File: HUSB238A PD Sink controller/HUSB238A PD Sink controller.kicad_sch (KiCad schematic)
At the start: 28 parts, among them J1 Power out header, J2 VSET, J3 Power out terminal, J4 ISET, J6 I2C, Q1 PMOS, U1 SRV05-4, U2 HUSB238A-xxxxx-QN16R

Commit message: R2.3
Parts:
- removed J1: Power out header, Connector_PinHeader_2.54mm:PinHeader_1x02_P2.54mm_Vertical, symbol Connector:Conn_01x02_Pin
- removed Q1: PMOS, symbol Simulation_SPICE:PMOS
- removed U1: SRV05-4, Package_TO_SOT_SMD:SOT-23-6, symbol Power_Protection:SRV05-4
- added D1: ≥48V TVS Clamp, Diode_SMD:D_SOD-123F, symbol Device:D_TVS_Small
- added Q1: CJAC70P06, Package_DFN_QFN:PQFN-8-EP_6x5mm_P1.27mm_Generic, symbol CJAC70P06:CJAC70P06
- added R4: 900kΩ, Resistor_SMD:R_0603_1608Metric, symbol Device:R_Small
- added U1: TPD4E05U06DQA, Package_SON:USON-10_2.5x1.0mm_P0.5mm, symbol Power_Protection:TPD4E05U06DQA
- C1: footprint Capacitor_SMD:C_1206_3216Metric_Pad1.33x1.80mm_HandSolder -> Capacitor_SMD:C_0603_1608Metric; LCSC Part # (none) -> C15849
- D2: renamed from D1; value ~ -> 15V; footprint Diode_SMD:D_1206_3216Metric_Pad1.42x1.75mm_HandSolder -> Diode_SMD:D_SOD-323
- J1: renamed from J3; value Power out terminal -> VBUS
- JP1: renamed from JP3; value I2C Mode -> I2C Enabled
- R1: value ~ -> 100kΩ; footprint Resistor_SMD:R_1206_3216Metric_Pad1.30x1.75mm_HandSolder -> Resistor_SMD:R_0603_1608Metric; LCSC Part # (none) -> C25803
- R12: renamed from R13; LCSC Part # (none) -> C74154
- R13: renamed from R12; LCSC Part # (none) -> C43670
- R14: renamed from R11; LCSC Part # (none) -> C229764
- R15: renamed from R10; LCSC Part # (none) -> C18012
- R16: renamed from R9; LCSC Part # (none) -> C17888
- R2: value ~ -> 20kΩ; footprint Resistor_SMD:R_1206_3216Metric_Pad1.30x1.75mm_HandSolder -> Resistor_SMD:R_0603_1608Metric; LCSC Part # (none) -> C4184
- R3: renamed from R15; footprint Resistor_SMD:R_1206_3216Metric_Pad1.30x1.75mm_HandSolder -> Resistor_SMD:R_0603_1608Metric; LCSC Part # (none) -> C22935
- R5: renamed from R3; LCSC Part # (none) -> C17888
- R6: renamed from R4; LCSC Part # (none) -> C18012
- R7: renamed from R5; LCSC Part # (none) -> C229764
- R8: renamed from R6; LCSC Part # (none) -> C43670
- R9: renamed from R7; LCSC Part # (none) -> C74154
- U2: value HUSB238A-xxxxx-QN16R -> HUSB238A; LCSC Part # (none) -> C24833806
- USBC1: LCSC Part # (none) -> C2931470
- renumbered J6 to J3, R8 to R10, R14 to R11
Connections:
- net CC1: now also U1.4 (D2+), U1.7 (NC)
- net CC2: now also U1.5 (D2-), U1.6 (NC)
- net D+: now also U1.1 (D1+), U1.10 (NC)
- net D-: now also U1.2 (D1-), U1.9 (NC)
- net GND: now also J1.1 (Pin_1), JP2.3, D1.2 (A2), U1.3 (GND), U1.8 (GND); no longer J1.2 (Pin_2), JP2.1 (42H)
- net GPIO/I2C: now also R4.1; no longer JP1.2 (B)
- net VBUS: now also D1.1 (A1), Q1.1 (S), Q1.2 (S), Q1.3 (S)
- net VBUS_OUT: now also J1.2 (Pin_2), Q1.5 (D), Q1.6 (D), Q1.7 (D), Q1.8 (D); no longer J1.1 (Pin_1)
- net VDD: now also JP2.1; no longer JP2.3 (62H)
- net at D2.2 (A), R1.2, R2.1: now also Q1.4 (G)
- new net: JP1.2 (B), R4.2
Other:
- moved on the sheet: C1, J1, J3, JP1, R3, U2

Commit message: rev 2.3
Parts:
- D2: LCSC Part # (none) -> C41410799
- J2, J4: now left out of the parts list
- Q1: LCSC Part # C41410799 -> C2898279
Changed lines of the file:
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@@
 		(unit 1)
 		(exclude_from_sim no)
-		(in_bom yes)
+		(in_bom no)
 		(on_board yes)
 		(dnp no)
@@
 			)
 		)
-		(property "LCSC Part #" "C41410799"
+		(property "LCSC Part #" "C2898279"
 			(at 226.06 38.1 0)
 			(effects
@@
 		(unit 1)
 		(exclude_from_sim no)
-		(in_bom yes)
+		(in_bom no)
 		(on_board yes)
 		(dnp no)
@@
 		)
 		(property "Value" "15V"
-			(at 205.74 40.3859 90)
+			(at 205.994 41.148 90)
 			(effects
 				(font
@@
 			(at 208.28 39.37 0)
 			(effects
+				(font
+					(size 1.27 1.27)
+				)
+				(hide yes)
+			)
+		)
+		(property "LCSC Part #" "C41410799"
+			(at 208.28 39.37 0)
+			(effects

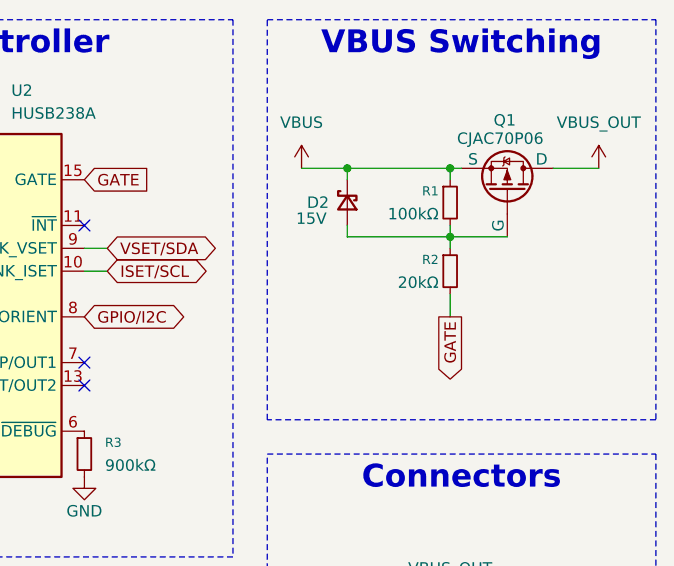
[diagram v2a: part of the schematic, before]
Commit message: Fix resistor values
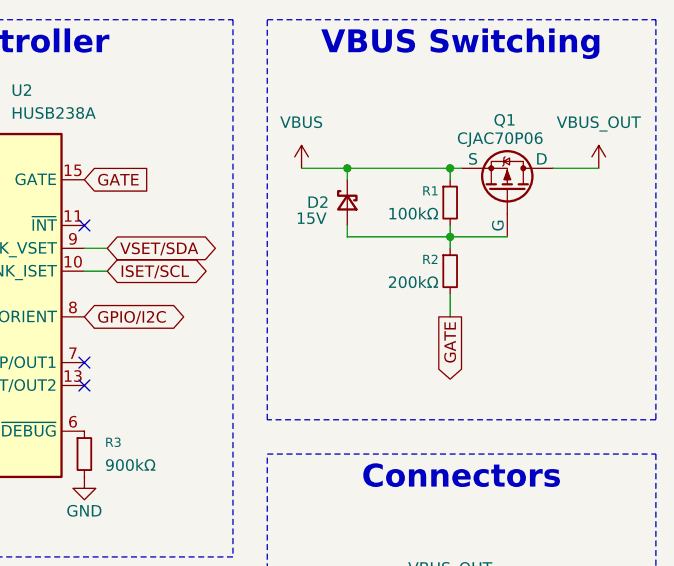
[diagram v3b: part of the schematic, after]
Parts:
- R2: value 20kΩ -> 200kΩ; LCSC Part # C4184 -> C25811
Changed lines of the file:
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@@
 			)
 		)
-		(property "Value" "20kΩ"
+		(property "Value" "200kΩ"
 			(at 218.44 48.26 0)
 			(effects
@@
 			)
 		)
-		(property "LCSC Part #" "C4184"
+		(property "LCSC Part #" "C25811"
 			(at 219.71 46.99 0)
 			(effects
